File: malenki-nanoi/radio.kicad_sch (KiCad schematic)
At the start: 22 parts, among them U1 A7105, Y1 16 Mhz 20ppm ABM10-16.000MHZ-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

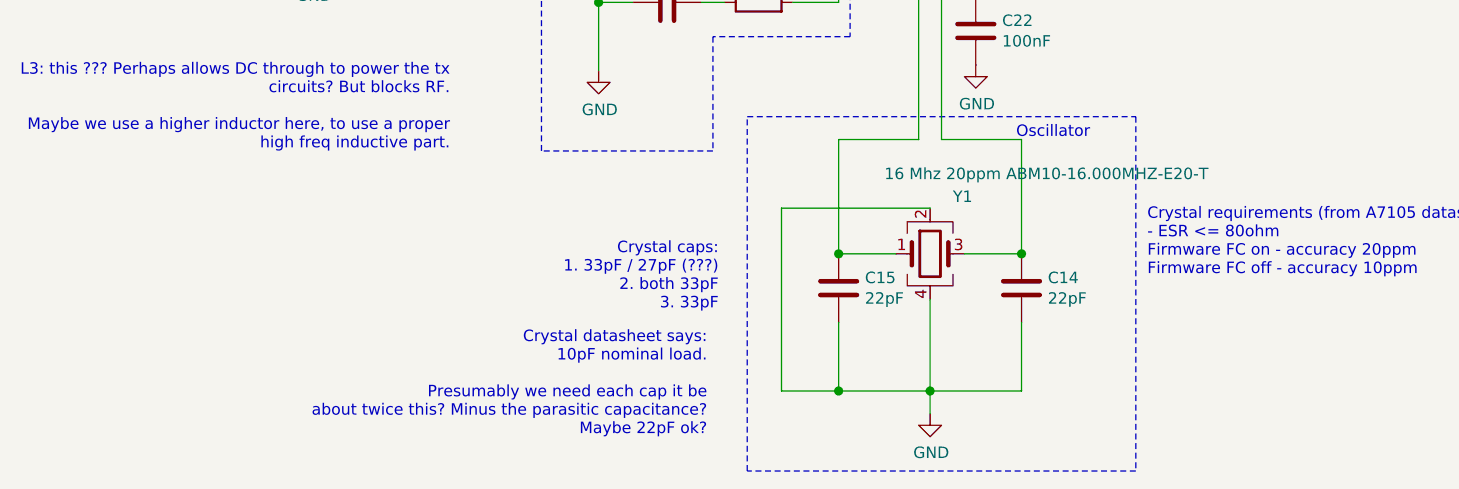
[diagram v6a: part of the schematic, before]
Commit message: Change crystal
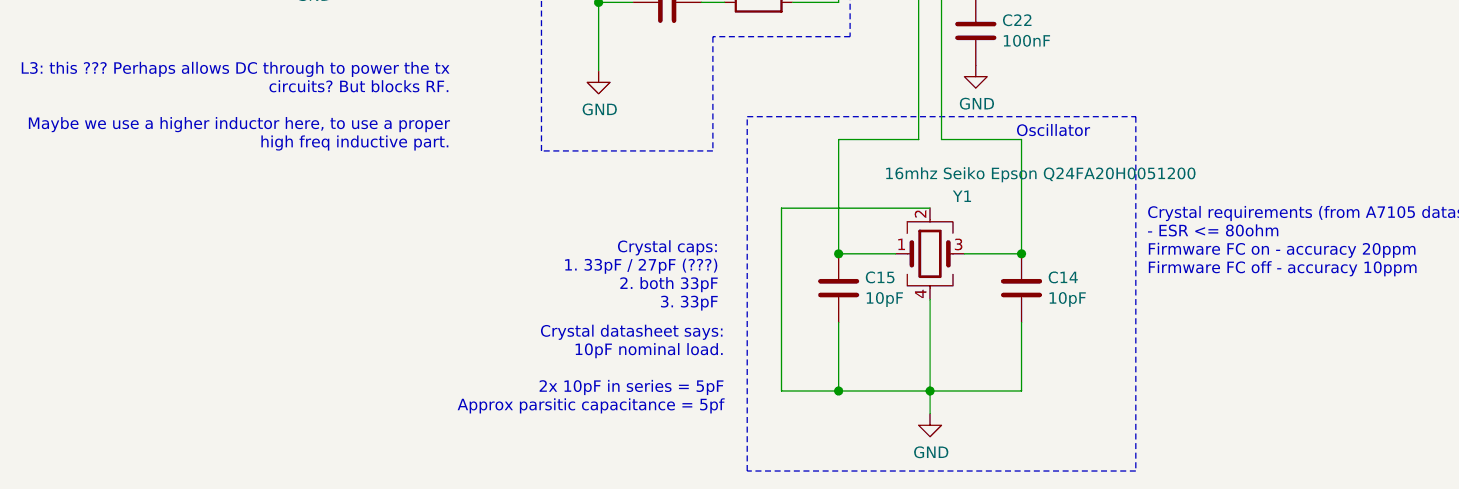
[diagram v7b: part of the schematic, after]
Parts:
- C14, C15: value 22pF -> 10pF
- Y1: value 16 Mhz 20ppm ABM10-16.000MHZ-E20-T -> 16mhz Seiko Epson Q24FA20H0051200; LCSC C179632 -> C255947
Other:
- note added: "Crystal datasheet says: 10pF nominal load. 2x 10pF in series = 5pF Approx parsitic capacitance = 5pf"
- note removed: "Crystal datasheet says: 10pF nominal load. Presumably we need each cap it be about twice this? Minus the parasitic capacitance? Maybe 22pF ok?"
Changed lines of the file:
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@@
-    (effects (font (size 1.27 1.27)) (justify right bottom))
-  )
-  (text "Crystal datasheet says:\n10pF nominal load.\n\nPresumably we need each cap it be\nabout twice this? Minus the parasitic capacitance?\nMaybe 22pF ok?"
-    (at 193.675 157.48 0)
     (effects (font (size 1.27 1.27)) (justify right bottom))
   )
   (text "Crystal caps:\n1. 33pF / 27pF (???)\n2. both 33pF\n3. 33pF"
     (at 194.945 143.51 0)
+    (effects (font (size 1.27 1.27)) (justify right bottom))
+  )
+  (text "Crystal datasheet says:\n10pF nominal load.\n\n2x 10pF in series = 5pF\nApprox parsitic capacitance = 5pf"
+    (at 195.58 154.94 0)
     (effects (font (size 1.27 1.27)) (justify right bottom))
   )
@@
       (effects (font (size 1.27 1.27)) (justify left))
     )
-    (property "Value" "22pF" (id 1) (at 211.201 142.113 0)
+    (property "Value" "10pF" (id 1) (at 211.201 142.113 0)
       (effects (font (size 1.27 1.27)) (justify left))
     )
@@
       (effects (font (size 1.27 1.27)) (justify left))
     )
-    (property "Value" "22pF" (id 1) (at 231.521 142.113 0)
+    (property "Value" "10pF" (id 1) (at 231.521 142.113 0)
       (effects (font (size 1.27 1.27)) (justify left))
     )
@@
       (effects (font (size 1.27 1.27)) (justify left))
     )
-    (property "Value" "16 Mhz 20ppm ABM10-16.000MHZ-E20-T " (id 1) (at 213.36 128.27 0)
+    (property "Value" "16mhz Seiko Epson Q24FA20H0051200 " (id 1) (at 213.36 128.27 0)
       (effects (font (size 1.27 1.27)) (justify left))
     )
@@
       (effects (font (size 1.27 1.27)) hide)
     )
-    (property "Datasheet" "https://datasheet.lcsc.com/szlcsc/1810170922_Abracon-LLC-ABM10-16-000MHZ-E20-T_C179632.pdf" (id 3) (at 218.44 137.16 0)
-      (effects (font (size 1.27 1.27)) hide)
-    )
-    (property "LCSC" "C179632" (id 4) (at 218.44 137.16 0)
-      (effects (font (size 1.27 1.27)) hide)
-    )
+    (property "Datasheet" "" (id 3) (at 218.44 137.16 0)
+      (effects (font (size 1.27 1.27)) hide)
+    )
+    (property "LCSC" "C255947" (id 4) (at 218.44 137.16 0)
+      (effects (font (size 1.27 1.27)) hide)
+    )

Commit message: Assign manufacturer part numbers and lcsc numbers
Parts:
- C10: LCSC (none) -> C1555; MPN (none) -> 0402CG220J500NT; Manufacturer (none) -> Guangdong Fenghua Advanced
- C11, C14, C15: LCSC (none) -> C32949; MPN (none) -> CL05C100JB5NNNC; Manufacturer (none) -> Samsung
- C12, C13, C16, C17, C22, C23: LCSC (none) -> C1525; MPN (none) -> CL05B104KO5NNNC; Manufacturer (none) -> Samsung
- C18: LCSC (none) -> C318606; MPN (none) -> CL05C561JB5NNNC; Manufacturer (none) -> Samsung
- C19: LCSC (none) -> C15195; MPN (none) -> CL05B103KB5NNNC; Manufacturer (none) -> Samsung
- C20, C21: LCSC (none) -> C12530; MPN (none) -> CL05A225MQ5NSNC; Manufacturer (none) -> Samsung
- C9: LCSC (none) -> C1550; MPN (none) -> 0402CG1R0C500NT; Manufacturer (none) -> Guangdong Fenghua Advanced
- L1: MPN (none) -> SDCL1608C2N7STDF; Manufacturer (none) -> Sunlord
- L2, L3: MPN (none) -> VHF160808H4N7ST; Manufacturer (none) -> Guangdong Fenghua
- R5: LCSC (none) -> C25087; MPN (none) -> 0402WGF2000TCE; Manufacturer (none) -> Uniroyal; Partnum (none) -> 10k
- U1: MPN (none) -> A71X05AQFI/Q; Manufacturer (none) -> AMICCOM
- Y1: MPN (none) -> Q24FA20H0051200; Manufacturer (none) -> Seiko Epson
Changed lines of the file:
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@@
+      (effects (font (size 1.27 1.27)) hide)
+    )
+    (property "MPN" "SDCL1608C2N7STDF" (id 4) (at 91.44 76.2 0)
+      (effects (font (size 1.27 1.27)) hide)
+    )
+    (property "Manufacturer" "Sunlord" (id 5) (at 91.44 76.2 0)
       (effects (font (size 1.27 1.27)) hide)
     )
@@
       (effects (font (size 1.27 1.27)) hide)
     )
+    (property "MPN" "VHF160808H4N7ST" (id 4) (at 113.03 94.615 0)
+      (effects (font (size 1.27 1.27)) hide)
+    )
+    (property "Manufacturer" "Guangdong Fenghua" (id 5) (at 113.03 94.615 0)
+      (effects (font (size 1.27 1.27)) hide)
+    )
   )
   (symbol (lib_id "Device:L") (at 149.86 82.55 0) (unit 1)
@@
     )
     (property "LCSC" "C1030" (id 4) (at 149.86 82.55 0)
+      (effects (font (size 1.27 1.27)) hide)
+    )
+    (property "MPN" "VHF160808H4N7ST" (id 4) (at 149.86 82.55 0)
+      (effects (font (size 1.27 1.27)) hide)
+    )
+    (property "Manufacturer" "Guangdong Fenghua" (id 5) (at 149.86 82.55 0)
       (effects (font (size 1.27 1.27)) hide)
     )
@@
       (effects (font (size 1.27 1.27)) hide)
     )
-    (property "LCSC" "" (id 4) (at 199.39 109.22 0)
+    (property "LCSC" "C25087" (id 4) (at 199.39 109.22 0)
+      (effects (font (size 1.27 1.27)) hide)
+    )
+    (property "MPN" "0402WGF2000TCE" (id 4) (at 199.39 109.22 0)
+      (effects (font (size 1.27 1.27)) hide)
+    )
+    (property "Manufacturer" "Uniroyal" (id 5) (at 199.39 109.22 0)
+      (effects (font (size 1.27 1.27)) hide)
+    )
+    (property "Partnum" "10k" (id 6) (at 199.39 109.22 0)
       (effects (font (size 1.27 1.27)) hide)
     )
@@
       (effects (font (size 1.27 1.27)) hide)
     )
-    (property "LCSC" "" (id 4) (at 99.06 80.01 0)
+    (property "LCSC" "C1550" (id 4) (at 99.06 80.01 0)
+      (effects (font (size 1.27 1.27)) hide)
+    )
+    (property "MPN" "0402CG1R0C500NT" (id 4) (at 99.06 80.01 0)
+      (effects (font (size 1.27 1.27)) hide)
+    )
+    (property "Manufacturer" "Guangdong Fenghua Advanced" (id 5) (at 99.06 80.01 0)
       (effects (font (size 1.27 1.27)) hide)
     )
@@
       (effects (font (size 1.27 1.27)) hide)
     )
-    (property "LCSC" "" (id 4) (at 128.27 76.2 0)
+    (property "LCSC" "C1555" (id 4) (at 128.27 76.2 0)
+      (effects (font (size 1.27 1.27)) hide)
+    )
+    (property "MPN" "0402CG220J500NT" (id 4) (at 128.27 76.2 0)
+      (effects (font (size 1.27 1.27)) hide)
+    )
+    (property "Manufacturer" "Guangdong Fenghua Advanced" (id 5) (at 128.27 76.2 0)
       (effects (font (size 1.27 1.27)) hide)
     )
@@
       (effects (font (size 1.27 1.27)) hide)
     )
-    (property "LCSC" "" (id 4) (at 128.27 83.82 0)
+    (property "LCSC" "C32949" (id 4) (at 128.27 83.82 0)
+      (effects (font (size 1.27 1.27)) hide)
+    )
+    (property "MPN" "CL05C100JB5NNNC" (id 4) (at 128.27 83.82 0)
+      (effects (font (size 1.27 1.27)) hide)
+    )
+    (property "Manufacturer" "Samsung" (id 5) (at 128.27 83.82 0)
       (effects (font (size 1.27 1.27)) hide)
     )
@@
       (effects (font (size 1.27 1.27)) hide)
     )
-    (property "LCSC" "" (id 4) (at 144.78 64.77 0)
+    (property "LCSC" "C1525" (id 4) (at 144.78 64.77 0)
+      (effects (font (size 1.27 1.27)) hide)
+    )
+    (property "MPN" "CL05B104KO5NNNC" (id 4) (at 144.78 64.77 0)
+      (effects (font (size 1.27 1.27)) hide)
+    )
+    (property "Manufacturer" "Samsung" (id 5) (at 144.78 64.77 0)
       (effects (font (size 1.27 1.27)) hide)
     )
@@
       (effects (font (size 1.27 1.27)) hide)
     )
-    (property "LCSC" "" (id 4) (at 149.86 100.33 0)
+    (property "LCSC" "C1525" (id 4) (at 149.86 100.33 0)
+      (effects (font (size 1.27 1.27)) hide)
+    )
+    (property "MPN" "CL05B104KO5NNNC" (id 4) (at 149.86 100.33 0)
+      (effects (font (size 1.27 1.27)) hide)
+    )
+    (property "Manufacturer" "Samsung" (id 5) (at 149.86 100.33 0)
       (effects (font (size 1.27 1.27)) hide)
     )
@@
       (effects (font (size 1.27 1.27)) hide)
     )
-    (property "LCSC" "" (id 4) (at 162.56 88.9 0)
+    (property "LCSC" "C1525" (id 4) (at 162.56 88.9 0)
+      (effects (font (size 1.27 1.27)) hide)
+    )
+    (property "MPN" "CL05B104KO5NNNC" (id 4) (at 162.56 88.9 0)
+      (effects (font (size 1.27 1.27)) hide)
+    )
+    (property "Manufacturer" "Samsung" (id 5) (at 162.56 88.9 0)
       (effects (font (size 1.27 1.27)) hide)
     )
@@
       (effects (font (size 1.27 1.27)) hide)
     )
-    (property "LCSC" "" (id 4) (at 177.8 64.77 0)
+    (property "LCSC" "C1525" (id 4) (at 177.8 64.77 0)
+      (effects (font (size 1.27 1.27)) hide)
+    )
+    (property "MPN" "CL05B104KO5NNNC" (id 4) (at 177.8 64.77 0)
+      (effects (font (size 1.27 1.27)) hide)
+    )
+    (property "Manufacturer" "Samsung" (id 5) (at 177.8 64.77 0)
       (effects (font (size 1.27 1.27)) hide)
     )
@@
       (effects (font (size 1.27 1.27)) hide)
     )
-    (property "LCSC" "" (id 4) (at 189.23 100.33 0)
+    (property "LCSC" "C318606" (id 4) (at 189.23 100.33 0)
+      (effects (font (size 1.27 1.27)) hide)
+    )
+    (property "MPN" "CL05C561JB5NNNC" (id 4) (at 189.23 100.33 0)
+      (effects (font (size 1.27 1.27)) hide)
+    )
+    (property "Manufacturer" "Samsung" (id 5) (at 189.23 100.33 0)
       (effects (font (size 1.27 1.27)) hide)
     )
@@
       (effects (font (size 1.27 1.27)) hide)
     )
-    (property "LCSC" "" (id 4) (at 189.23 109.22 0)
+    (property "LCSC" "C15195" (id 4) (at 189.23 109.22 0)
+      (effects (font (size 1.27 1.27)) hide)
+    )
+    (property "MPN" "CL05B103KB5NNNC" (id 4) (at 189.23 109.22 0)
+      (effects (font (size 1.27 1.27)) hide)
+    )
+    (property "Manufacturer" "Samsung" (id 5) (at 189.23 109.22 0)
       (effects (font (size 1.27 1.27)) hide)
     )
@@
       (effects (font (size 1.27 1.27)) hide)
     )
-    (property "LCSC" "" (id 4) (at 196.85 59.69 0)
+    (property "LCSC" "C12530" (id 4) (at 196.85 59.69 0)
+      (effects (font (size 1.27 1.27)) hide)
+    )
+    (property "MPN" "CL05A225MQ5NSNC" (id 4) (at 196.85 59.69 0)
+      (effects (font (size 1.27 1.27)) hide)
+    )
+    (property "Manufacturer" "Samsung" (id 5) (at 196.85 59.69 0)
       (effects (font (size 1.27 1.27)) hide)
     )
@@
       (effects (font (size 1.27 1.27)) hide)
     )
-    (property "LCSC" "" (id 4) (at 203.2 45.72 0)
+    (property "LCSC" "C12530" (id 4) (at 203.2 45.72 0)
+      (effects (font (size 1.27 1.27)) hide)
+    )
+    (property "MPN" "CL05A225MQ5NSNC" (id 4) (at 203.2 45.72 0)
+      (effects (font (size 1.27 1.27)) hide)
+    )
+    (property "Manufacturer" "Samsung" (id 5) (at 203.2 45.72 0)
       (effects (font (size 1.27 1.27)) hide)
     )
@@
       (effects (font (size 1.27 1.27)) hide)
     )
-    (property "LCSC" "" (id 4) (at 208.28 140.97 0)
+    (property "LCSC" "C32949" (id 4) (at 208.28 140.97 0)
+      (effects (font (size 1.27 1.27)) hide)
+    )
+    (property "MPN" "CL05C100JB5NNNC" (id 4) (at 208.28 140.97 0)
+      (effects (font (size 1.27 1.27)) hide)
+    )
+    (property "Manufacturer" "Samsung" (id 5) (at 208.28 140.97 0)
       (effects (font (size 1.27 1.27)) hide)
     )
@@
       (effects (font (size 1.27 1.27)) hide)
     )
-    (property "LCSC" "" (id 4) (at 223.52 112.395 0)
+    (property "LCSC" "C1525" (id 4) (at 223.52 112.395 0)
+      (effects (font (size 1.27 1.27)) hide)
+    )
+    (property "MPN" "CL05B104KO5NNNC" (id 4) (at 223.52 112.395 0)
+      (effects (font (size 1.27 1.27)) hide)
+    )
+    (property "Manufacturer" "Samsung" (id 5) (at 223.52 112.395 0)
       (effects (font (size 1.27 1.27)) hide)
     )
@@
       (effects (font (size 1.27 1.27)) hide)
     )
-    (property "LCSC" "" (id 4) (at 228.6 140.97 0)
+    (property "LCSC" "C32949" (id 4) (at 228.6 140.97 0)
+      (effects (font (size 1.27 1.27)) hide)
+    )
+    (property "MPN" "CL05C100JB5NNNC" (id 4) (at 228.6 140.97 0)
+      (effects (font (size 1.27 1.27)) hide)
+    )
+    (property "Manufacturer" "Samsung" (id 5) (at 228.6 140.97 0)
       (effects (font (size 1.27 1.27)) hide)
     )
@@
       (effects (font (size 1.27 1.27)) hide)
     )
-    (property "LCSC" "" (id 4) (at 243.84 83.82 0)
+    (property "LCSC" "C1525" (id 4) (at 243.84 83.82 0)
+      (effects (font (size 1.27 1.27)) hide)
+    )
+    (property "MPN" "CL05B104KO5NNNC" (id 4) (at 243.84 83.82 0)
+      (effects (font (size 1.27 1.27)) hide)
+    )
+    (property "Manufacturer" "Samsung" (id 5) (at 243.84 83.82 0)
       (effects (font (size 1.27 1.27)) hide)
     )
@@
       (effects (font (size 1.27 1.27)) hide)
     )
+    (property "MPN" "Q24FA20H0051200" (id 4) (at 218.44 137.16 0)
+      (effects (font (size 1.27 1.27)) hide)
+    )
+    (property "Manufacturer" "Seiko Epson" (id 5) (at 218.44 137.16 0)
+      (effects (font (size 1.27 1.27)) hide)
+    )
   )
   (symbol (lib_id "malenki-nanoi:A7105") (at 217.17 76.2 0) (unit 1)
@@
       (effects (font (size 1.27 1.27)) hide)
     )
+    (property "MPN" "A71X05AQFI/Q" (id 4) (at 217.17 76.2 0)
+      (effects (font (size 1.27 1.27)) hide)
+    )
+    (property "Manufacturer" "AMICCOM" (id 5) (at 217.17 76.2 0)
+      (effects (font (size 1.27 1.27)) hide)
+    )
